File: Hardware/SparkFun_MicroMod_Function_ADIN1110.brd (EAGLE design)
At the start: 38 x 65 mm, 115 parts, among them J1 T1_INDUSTRIAL, J2 MICROMOD_FUNCTION_STANDARD, Q1 220mA/50V/3.5Ω, Q2 20V/4.2A/52mΩ/1.4W, T1 WE-STST, U1 ADIN1110, U2 EEPROM, U3 3.3V, U4 WE-TVS, Y1 25MHz

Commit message: Wurth Electronik caps
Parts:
- C21: value 0.1uF/50V -> 0.1uF
- C22: value 0.1uF/100V -> 0.1uF

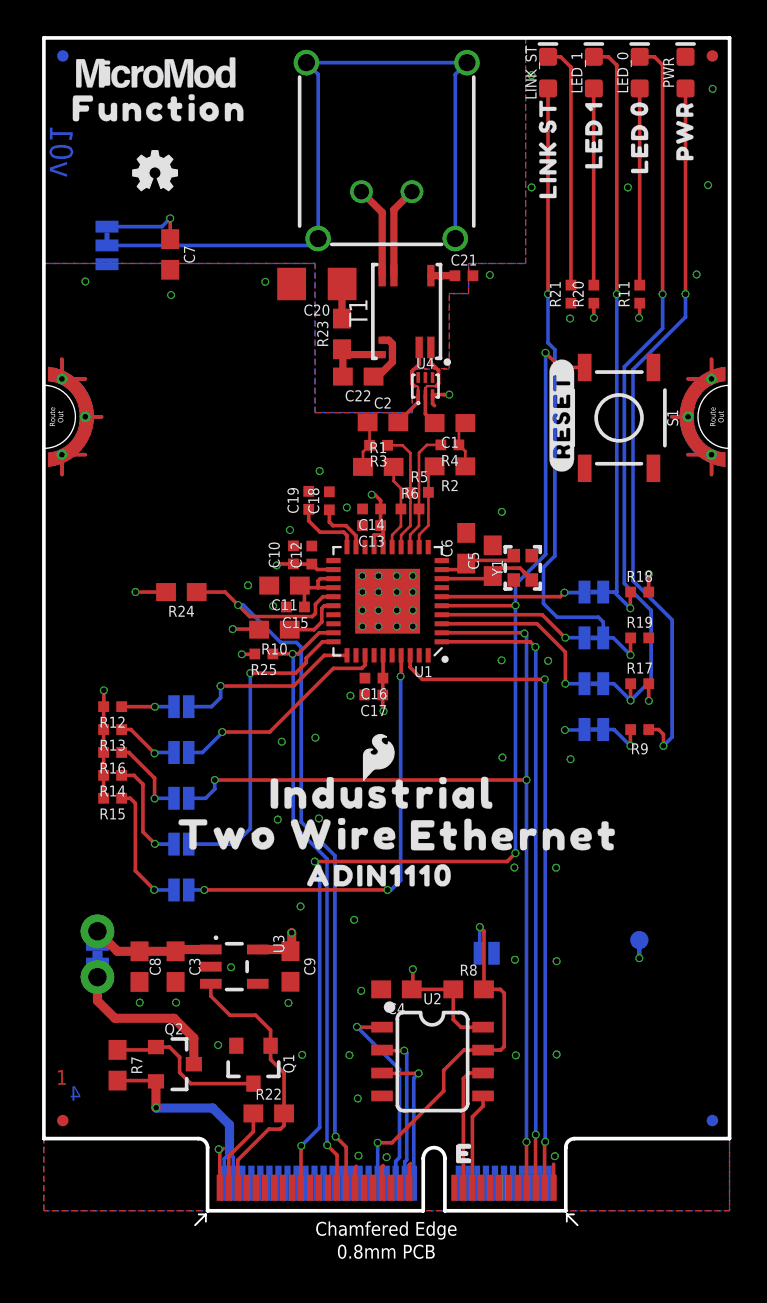
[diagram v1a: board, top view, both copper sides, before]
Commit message: LEDs and Xtal swapped out for Wurth Electronic Parts
Also bumped version to v10, because the WE xtal has GND pads, and new package has polarity dot.
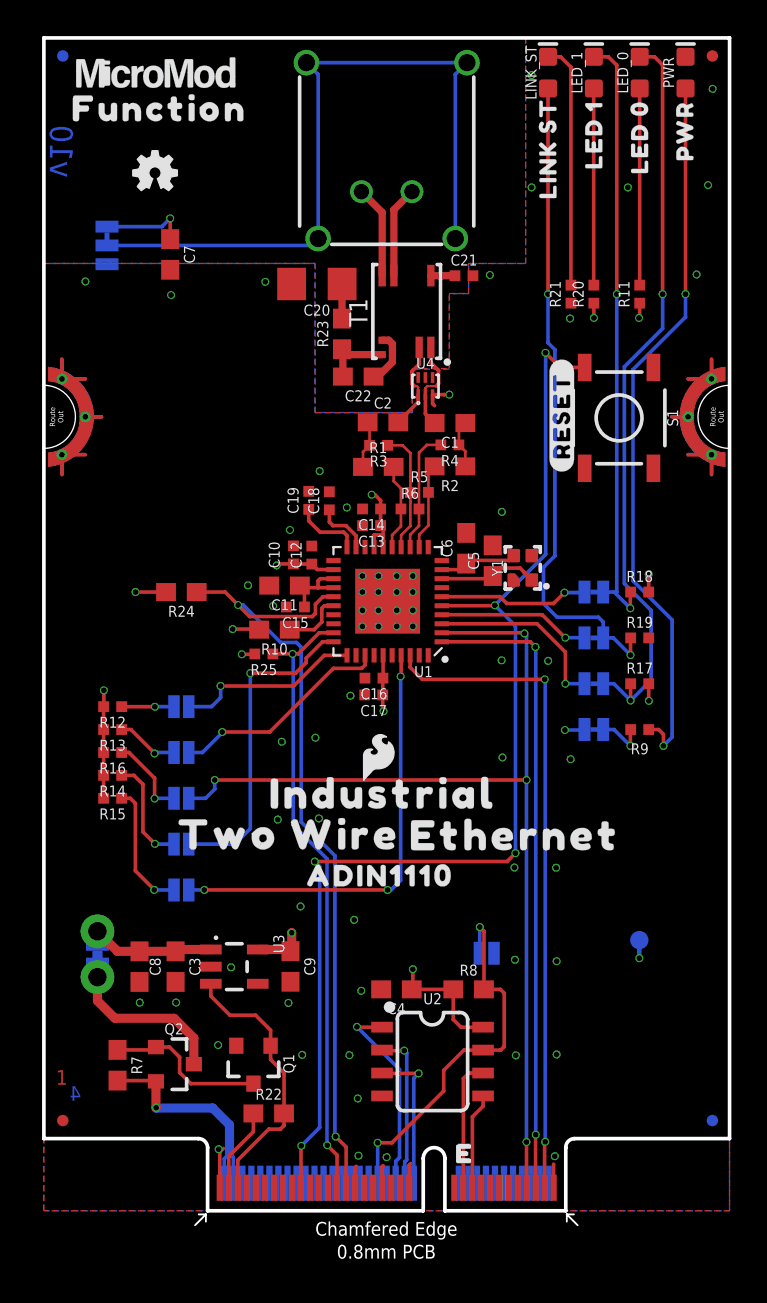
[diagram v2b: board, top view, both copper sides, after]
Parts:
- Y1: device SparkFun-Clocks:CRYSTAL-SMD-2.0X1.6MM -> SparkFun-Clocks:CRYSTAL-SMD-2.0X1.6MM-WE
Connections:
- net GND: now also Y1.2, Y1.4
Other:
- board text added: "v10"
- board text removed: "v01"
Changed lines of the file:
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@@
 <plain>
 <wire x1="28.925" y1="0" x2="22.225" y2="0" width="0.2032" layer="20"/>
-<text x="0.9686" y="58.713278125" size="1.27" layer="16" font="vector" ratio="20" rot="SMR90" align="center">v01</text>
+<text x="0.9686" y="58.713278125" size="1.27" layer="16" font="vector" ratio="20" rot="SMR90" align="center">v10</text>
 <text x="19.95" y="-14.77" size="1.778" layer="51" font="vector" ratio="10">Pete Lewis</text>
 <wire x1="21.025" y1="0" x2="9.075" y2="0" width="0.2032" layer="20"/>
@@
 </element>
 <element name="LOGO2" library="SparkFun-Aesthetics" package="ORDERING_INSTRUCTIONS" value="SPECIAL_INSTRUCTIONS-ORDERING" x="45.72" y="60.96" smashed="yes"/>
-<element name="Y1" library="SparkFun-Clocks" package="CRYSTAL-SMD-2.0X1.6MM" value="25MHz" x="26.54" y="35.632" smashed="yes" rot="R90">
+<element name="Y1" library="SparkFun-Clocks" package="CRYSTAL-SMD-2.0X1.6MM-WE" value="25MHz" x="26.54" y="35.632" smashed="yes" rot="R90">
 <attribute name="NAME" x="25.44" y="35.632" size="0.6096" layer="25" ratio="20" rot="R90" align="bottom-center"/>
-<attribute name="PROD_ID" value="XTAL-16235" x="26.54" y="35.632" size="1.778" layer="27" font="vector" ratio="15" rot="R90" display="off"/>
+<attribute name="PROD_ID" value="XTAL-16515" x="26.54" y="35.632" size="1.778" layer="27" font="vector" ratio="15" rot="R90" display="off"/>
 <attribute name="VALUE" value="25MHz" x="27.7749" y="35.412678125" size="0.6096" layer="27" ratio="20" rot="R90" align="top-center"/>
 </element>
@@
 <element name="PWR" library="SparkFun-LED" package="LED-0603" value="Red" x="35.560040625" y="63.0764" smashed="yes" rot="R90">
 <attribute name="NAME" x="34.925040625" y="63.0764" size="0.6096" layer="25" font="vector" ratio="20" rot="R90" align="bottom-center"/>
-<attribute name="PROD_ID" value="DIO-00819" x="32.560040625" y="59.0764" size="1.778" layer="27" font="vector" ratio="15" rot="R90" display="off"/>
-<attribute name="VALUE" x="36.195040625" y="63.0764" size="0.6096" layer="27" font="vector" ratio="20" rot="R90" align="top-center"/>
+<attribute name="PROD_ID" value="DIO-16511" x="32.560040625" y="59.0764" size="1.778" layer="27" font="vector" ratio="15" rot="R90" display="off"/>
+<attribute name="VALUE" value="Red" x="36.195040625" y="63.0764" size="0.6096" layer="27" font="vector" ratio="20" rot="R90" align="top-center"/>
 </element>
 <element name="TP1" library="SparkFun-Connectors" package="PAD.03X.04" value="TEST-POINT3X4" x="33" y="15" smashed="yes" rot="MR0"/>
@@
 <element name="LED_0" library="SparkFun-LED" package="LED-0603" value="Green" x="33.020040625" y="63.0764" smashed="yes" rot="R90">
 <attribute name="NAME" x="32.385040625" y="63.0764" size="0.6096" layer="25" font="vector" ratio="20" rot="R90" align="bottom-center"/>
-<attribute name="PROD_ID" value="DIO-00821" x="33.020040625" y="63.0764" size="1.778" layer="27" font="vector" ratio="15" rot="R90" display="off"/>
-<attribute name="VALUE" x="33.655040625" y="63.0764" size="0.6096" layer="27" font="vector" ratio="20" rot="R90" align="top-center"/>
+<attribute name="PROD_ID" value="DIO-16512" x="33.020040625" y="63.0764" size="1.778" layer="27" font="vector" ratio="15" rot="R90" display="off"/>
+<attribute name="VALUE" value="Green" x="33.655040625" y="63.0764" size="0.6096" layer="27" font="vector" ratio="20" rot="R90" align="top-center"/>
 </element>
 <element name="R11" library="SparkFun-Resistors" package="0402-TIGHT" value="1k" x="33.02" y="50.8" smashed="yes" rot="R90">
@@
 <element name="LED_1" library="SparkFun-LED" package="LED-0603" value="Yellow" x="30.480040625" y="63.0764" smashed="yes" rot="R90">
 <attribute name="NAME" x="29.845040625" y="63.0764" size="0.6096" layer="25" font="vector" ratio="20" rot="R90" align="bottom-center"/>
-<attribute name="PROD_ID" value="DIO-09003" x="30.480040625" y="63.0764" size="1.778" layer="27" font="vector" ratio="15" rot="R90" display="off"/>
+<attribute name="PROD_ID" value="DIO-16514" x="30.480040625" y="63.0764" size="1.778" layer="27" font="vector" ratio="15" rot="R90" display="off"/>
 <attribute name="VALUE" x="31.115040625" y="63.0764" size="0.6096" layer="27" font="vector" ratio="20" rot="R90" align="top-center"/>
 </element>
@@
 <element name="LINK_ST" library="SparkFun-LED" package="LED-0603" value="Blue" x="27.940040625" y="63.0764" smashed="yes" rot="R90">
 <attribute name="NAME" x="27.305040625" y="63.0764" size="0.6096" layer="25" font="vector" ratio="20" rot="R90" align="bottom-center"/>
-<attribute name="PROD_ID" value="DIO-08575" x="27.940040625" y="63.0764" size="1.778" layer="27" font="vector" ratio="15" rot="R90" display="off"/>
-<attribute name="VALUE" x="28.575040625" y="63.0764" size="0.6096" layer="27" font="vector" ratio="20" rot="R90" align="top-center"/>
+<attribute name="PROD_ID" value="DIO-16513" x="27.940040625" y="63.0764" size="1.778" layer="27" font="vector" ratio="15" rot="R90" display="off"/>
+<attribute name="VALUE" value="Blue" x="28.575040625" y="63.0764" size="0.6096" layer="27" font="vector" ratio="20" rot="R90" align="top-center"/>
 </element>
 <element name="R5" library="SparkFun-Resistors" package="0402-TIGHT" value="10.2Ω" x="20.812759375" y="39.8145" smashed="yes">
@@
 <via x="27.03068125" y="56.71565625" extent="1-16" drill="0.3048"/>
 <via x="32.36468125" y="56.71565625" extent="1-16" drill="0.3048"/>
+<contactref element="Y1" pad="2"/>
+<contactref element="Y1" pad="4"/>
 </signal>
 <signal name="3.3V">
@@
 <contactref element="U1" pad="5"/>
 <contactref element="S1" pad="3"/>
-<wire x1="22.05" y1="33.532" x2="26.117053125" y2="33.532" width="0.2032" layer="1"/>
-<wire x1="26.117053125" y1="33.532" x2="26.139021875" y2="33.55396875" width="0.2032" layer="1"/>
-<via x="26.139021875" y="33.55396875" extent="1-16" drill="0.3048"/>
+<wire x1="22.05" y1="33.532" x2="24.974053125" y2="33.532" width="0.2032" layer="1"/>
+<wire x1="24.974053125" y1="33.532" x2="24.996021875" y2="33.55396875" width="0.2032" layer="1"/>
+<via x="24.996021875" y="33.55396875" extent="1-16" drill="0.3048"/>
 <wire x1="27.8003" y1="47.551340625" x2="27.810140625" y2="47.5415" width="0.2032" layer="16"/>
 <wire x1="27.810140625" y1="47.5415" x2="27.810140625" y2="36.378246875" width="0.2032" layer="16"/>
-<wire x1="26.139021875" y1="33.55396875" x2="26.139021875" y2="34.707128125" width="0.2032" layer="16"/>
-<wire x1="27.810140625" y1="36.378246875" x2="26.139021875" y2="34.707128125" width="0.2032" layer="16"/>
+<wire x1="24.996021875" y1="33.55396875" x2="24.996021875" y2="33.564128125" width="0.2032" layer="16"/>
+<wire x1="27.810140625" y1="36.378246875" x2="24.996021875" y2="33.564128125" width="0.2032" layer="16"/>
 <via x="27.8003" y="47.551340625" extent="1-16" drill="0.3048"/>
 <wire x1="27.8003" y1="47.551340625" x2="28.615640625" y2="46.736" width="0.2032" layer="1"/>
@@
 <via x="26.134059375" y="19.81961875" extent="1-16" drill="0.3048"/>
 <wire x1="15.28571875" y1="4.615178125" x2="15.28571875" y2="19.08048125" width="0.2032" layer="16"/>
-<wire x1="26.134059375" y1="33.54900625" x2="26.139021875" y2="33.55396875" width="0.2032" layer="16"/>
-<wire x1="26.134059375" y1="19.81961875" x2="26.134059375" y2="33.54900625" width="0.2032" layer="16"/>
+<wire x1="26.134059375" y1="32.41593125" x2="24.996021875" y2="33.55396875" width="0.2032" layer="16"/>
+<wire x1="26.134059375" y1="19.81961875" x2="26.134059375" y2="32.41593125" width="0.2032" layer="16"/>
 </signal>
 <signal name="1.1V">
@@
 <contactref element="U1" pad="6"/>
 <contactref element="LED-1" pad="2"/>
-<wire x1="22.05" y1="34.032" x2="28.622" y2="34.032" width="0.2032" layer="1"/>
+<wire x1="22.05" y1="34.032" x2="25.277" y2="34.032" width="0.2032" layer="1"/>
+<wire x1="25.277" y1="34.032" x2="25.654" y2="33.655" width="0.2032" layer="1"/>
 <via x="28.85" y="34.26" extent="1-16" drill="0.3048"/>
 <wire x1="28.85" y1="34.26" x2="29.9293" y2="34.26" width="0.2032" layer="16"/>
 <wire x1="29.9293" y1="34.26" x2="29.9593" y2="34.29" width="0.2032" layer="16"/>
-<wire x1="28.622" y1="34.032" x2="28.85" y2="34.26" width="0.2032" layer="1"/>
+<wire x1="25.654" y1="33.655" x2="28.245" y2="33.655" width="0.2032" layer="1"/>
+<wire x1="28.245" y1="33.655" x2="28.85" y2="34.26" width="0.2032" layer="1"/>
 </signal>
 <signal name="N$33">

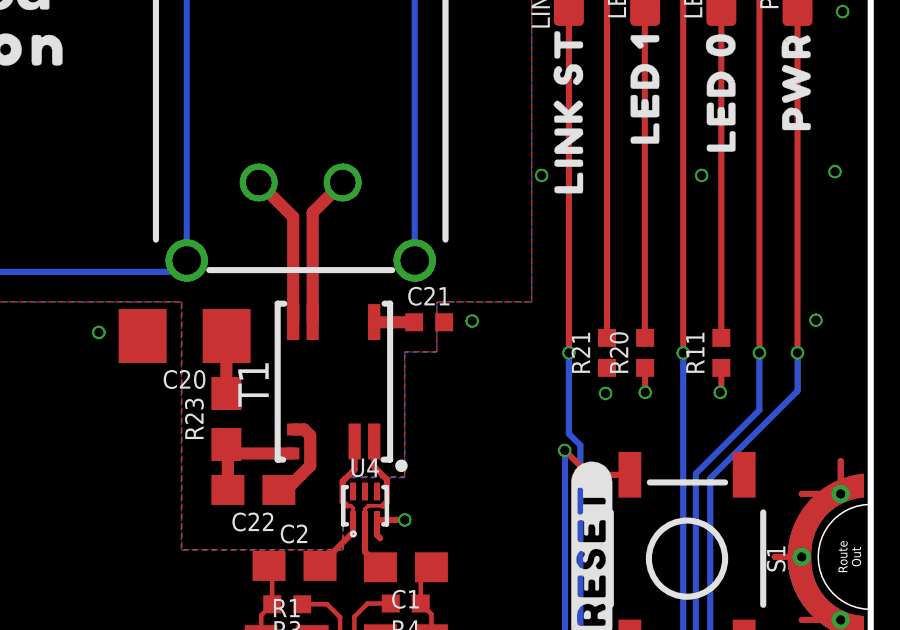
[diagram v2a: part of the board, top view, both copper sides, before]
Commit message: Switched C21 from 0402 to 0603 package
Due to sourcing issues.
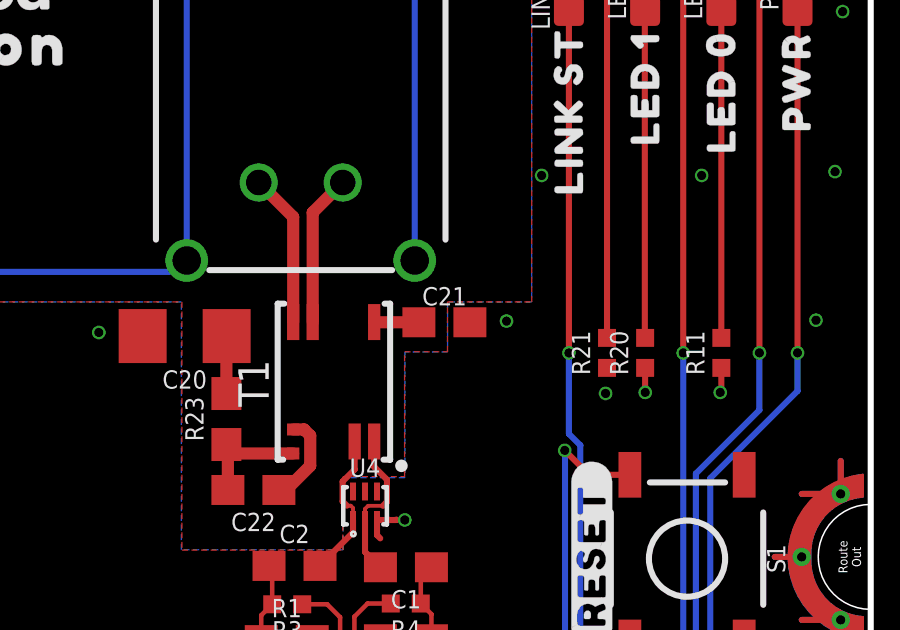
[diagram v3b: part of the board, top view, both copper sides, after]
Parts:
- C21: device SparkFun-Capacitors:0402-TIGHT -> SparkFun-Capacitors:0603
- moved C21 0.51 mm to (23.8, 51.8)
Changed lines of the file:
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@@
 <setting verticaltext="up"/>
 </settings>
-<grid distance="0.05" unitdist="inch" unit="inch" style="lines" multiple="1" display="yes" altdistance="0.005" altunitdist="inch" altunit="inch"/>
+<grid distance="0.05" unitdist="inch" unit="inch" style="lines" multiple="1" display="yes" altdistance="0.001" altunitdist="inch" altunit="inch"/>
 <layers>
 <layer number="1" name="Top/Horz" color="4" fill="1" visible="yes" active="yes"/>
-<layer number="2" name="Route2" color="1" fill="3" visible="no" active="yes"/>
-<layer number="15" name="Route15" color="4" fill="6" visible="no" active="yes"/>
+<layer number="2" name="Route2" color="1" fill="3" visible="yes" active="yes"/>
+<layer number="15" name="Route15" color="4" fill="6" visible="yes" active="yes"/>
 <layer number="16" name="Bottom/Vert" color="1" fill="1" visible="yes" active="yes"/>
 <layer number="17" name="Pads" color="2" fill="1" visible="yes" active="yes"/>
@@
 <attribute name="VALUE" value="100" x="15.10791875" y="48.493678125" size="0.6096" layer="27" font="vector" ratio="20" rot="R90" align="top-center"/>
 </element>
-<element name="C21" library="SparkFun-Capacitors" package="0402-TIGHT" value="0.1uF" x="23.2816375" y="51.821078125" smashed="yes">
-<attribute name="NAME" x="23.2816375" y="52.383078125" size="0.6096" layer="25" font="vector" ratio="20" align="bottom-center"/>
-<attribute name="PROD_ID" value="CAP-16431" x="23.2816375" y="51.821078125" size="1.778" layer="27" font="vector" ratio="15" display="off"/>
-<attribute name="VALUE" x="24.78531875" y="51.401315625" size="0.6096" layer="27" font="vector" ratio="20" align="top-center"/>
+<element name="C21" library="SparkFun-Capacitors" package="0603" value="0.1uF" x="23.7896375" y="51.821078125" smashed="yes">
+<attribute name="NAME" x="23.7896375" y="52.383078125" size="0.6096" layer="25" font="vector" ratio="20" align="bottom-center"/>
+<attribute name="PROD_ID" value="CAP-16523" x="23.7896375" y="51.821078125" size="1.778" layer="27" font="vector" ratio="15" display="off"/>
+<attribute name="VALUE" x="25.29331875" y="51.401315625" size="0.6096" layer="27" font="vector" ratio="20" align="top-center"/>
 </element>
 <element name="C22" library="SparkFun-Capacitors" package="0603" value="0.1uF" x="17.421859375" y="46.23054375" smashed="yes" rot="R180">
@@
 <vertex x="22.46121875" y="46.675040625"/>
 <vertex x="22.46121875" y="50.835559375"/>
-<vertex x="23.53818125" y="50.835559375"/>
-<vertex x="23.53818125" y="52.49903125"/>
+<vertex x="23.89378125" y="50.835559375"/>
+<vertex x="23.89378125" y="52.49903125"/>
 <vertex x="26.7" y="52.49903125"/>
 <vertex x="26.7" y="65"/>
@@
 <vertex x="26.7" y="65"/>
 <vertex x="26.7" y="52.498996875"/>
-<vertex x="23.53818125" y="52.498996875"/>
-<vertex x="23.53818125" y="50.83048125"/>
+<vertex x="23.89378125" y="52.498996875"/>
+<vertex x="23.89378125" y="50.83048125"/>
 <vertex x="22.47138125" y="50.83048125"/>
 <vertex x="22.47138125" y="46.64201875"/>
@@
 <vertex x="20.5" y="46.5"/>
 <vertex x="22.5" y="46.5"/>
-<vertex x="22.5" y="51"/>
-<vertex x="23.5" y="51"/>
-<vertex x="23.5" y="52.5"/>
+<vertex x="22.5" y="50.8222"/>
+<vertex x="23.881" y="50.8222"/>
+<vertex x="23.881" y="52.5"/>
 <vertex x="38" y="52.5"/>
 <vertex x="38" y="0"/>
@@
 <wire x1="35.560040625" y1="63.9534" x2="35.6666" y2="63.9534" width="0.2032" layer="1"/>
 <via x="29.161740625" y="49.44871875" extent="1-16" drill="0.3048"/>
-<via x="24.716740625" y="51.86171875" extent="1-16" drill="0.3048"/>
+<via x="25.859740625" y="51.86171875" extent="1-16" drill="0.3048"/>
 <via x="17.436459375" y="3.053003125" extent="1-16" drill="0.3048"/>
 <via x="28.316459375" y="3.023003125" extent="1-16" drill="0.3048"/>
@@
 <vertex x="20.5" y="46.5"/>
 <vertex x="22.5" y="46.5"/>
-<vertex x="22.5" y="51"/>
-<vertex x="23.5" y="51"/>
-<vertex x="23.5" y="52.5"/>
+<vertex x="22.5" y="50.8222"/>
+<vertex x="23.881" y="50.8222"/>
+<vertex x="23.881" y="52.5"/>
 <vertex x="38" y="52.5"/>
 <vertex x="38" y="0"/>
@@
 <contactref element="T1" pad="5"/>
 <contactref element="C21" pad="1"/>
-<wire x1="22.7816375" y1="51.821078125" x2="21.45528125" y2="51.821078125" width="0.4064" layer="1"/>
+<wire x1="22.9396375" y1="51.821078125" x2="21.45528125" y2="51.821078125" width="0.4064" layer="1"/>
 <wire x1="21.45528125" y1="51.821078125" x2="21.44901875" y2="51.827340625" width="0.4064" layer="1"/>
 </signal>

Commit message: Add Prod_IDs to T1 connectors
updated single and panel brd files
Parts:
- J1: value T1_INDUSTRIAL -> IP20(RJ50)
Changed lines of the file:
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@@
 <setting verticaltext="up"/>
 </settings>
-<grid distance="0.05" unitdist="inch" unit="inch" style="lines" multiple="1" display="yes" altdistance="0.001" altunitdist="inch" altunit="inch"/>
+<grid distance="0.05" unitdist="inch" unit="inch" style="lines" multiple="1" display="yes" altdistance="0.005" altunitdist="inch" altunit="inch"/>
 <layers>
 <layer number="1" name="Top/Horz" color="4" fill="1" visible="yes" active="yes"/>
-<layer number="2" name="Route2" color="1" fill="3" visible="yes" active="yes"/>
-<layer number="15" name="Route15" color="4" fill="6" visible="yes" active="yes"/>
+<layer number="2" name="Route2" color="1" fill="3" visible="no" active="yes"/>
+<layer number="15" name="Route15" color="4" fill="6" visible="no" active="yes"/>
 <layer number="16" name="Bottom/Vert" color="1" fill="1" visible="yes" active="yes"/>
 <layer number="17" name="Pads" color="2" fill="1" visible="yes" active="yes"/>
@@
 <element name="U$5" library="SparkFun-Aesthetics" package="SFE_LOGO_FLAME_.1" value="" x="18.542" y="25.146" smashed="yes"/>
 <element name="U$1" library="output" package="#RESET#0" value="" x="28.702" y="44.069" smashed="yes" rot="R90"/>
-<element name="J1" library="ADIN1110" package="T1_INDUSTRIAL_JACK_AH_IP20" value="T1_INDUSTRIAL" x="19" y="65" smashed="yes" rot="R180"/>
+<element name="J1" library="ADIN1110" package="T1_INDUSTRIAL_JACK_AH_IP20" value="IP20(RJ50)" x="19" y="65" smashed="yes" rot="R180">
+<attribute name="PROD_ID" value="CONN-16501" x="19" y="65" size="1.778" layer="27" rot="R180" display="off"/>
+<attribute name="VALUE" value="IP20(RJ50)" x="19" y="65" size="1.778" layer="27" rot="R180" display="off"/>
+</element>
 <element name="SHLD" library="SparkFun-Jumpers" package="SMT-JUMPER_3_1-NC_TRACE_SILK" package3d_urn="urn:adsk.eagle:package:39288/1" value="" x="3.5" y="53.5" smashed="yes" rot="MR90">
 <attribute name="NAME" x="4.643" y="53.5" size="0.6096" layer="26" font="vector" ratio="20" rot="MR90" align="bottom-center"/>
